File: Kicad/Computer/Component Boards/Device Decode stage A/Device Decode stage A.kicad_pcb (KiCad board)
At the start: 2 copper layers, 26.7 x 59.7 mm, 24 parts, among them IC1 AP7365-33WG-7, IC12 SN74LVC1G10DBVR, IC13 74LVC04APW,118, IC16 74LVC02APW,118, IC2 74LVC138APW-Q100J, IC3 74LVC02APW,118, IC4 74LVC1G32GV,125, IC5 74LVC02APW,118, IC7 SN74F521NSR, IC8 SN74F521NSR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

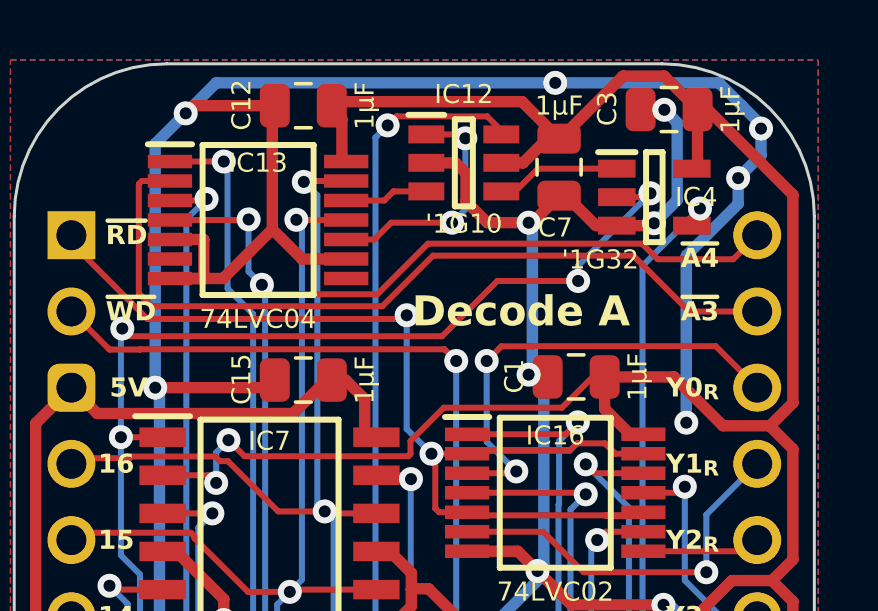
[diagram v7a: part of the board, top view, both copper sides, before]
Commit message: Resized 15mm wide boards and fixed GND pins.  Added GPIO 4bit and PS2 Board.
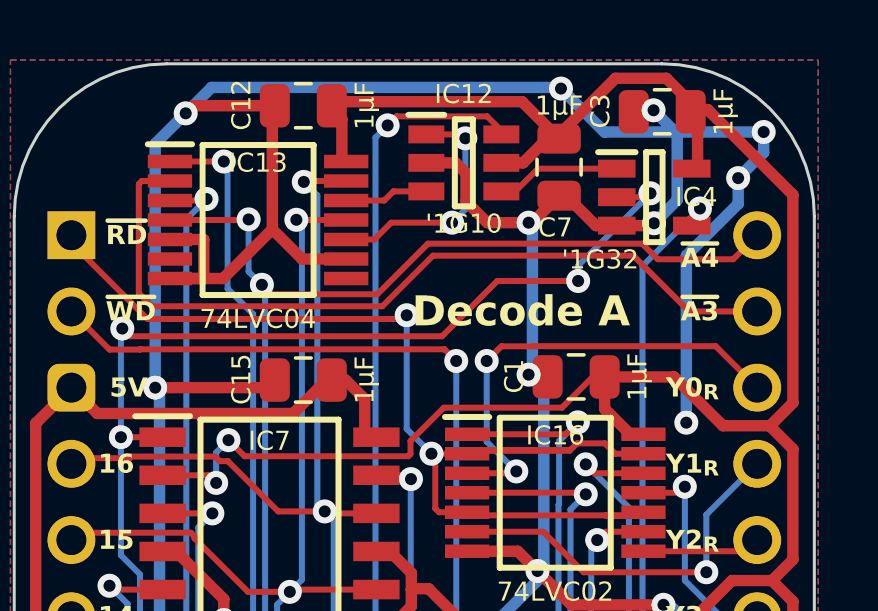
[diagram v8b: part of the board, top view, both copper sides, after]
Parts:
- moved C3 0.24 mm to (108.6, 54.3)
